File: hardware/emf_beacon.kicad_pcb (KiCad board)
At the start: 2 copper layers, 100 x 100 mm, 149 parts, among them J1 Conn_01x06, J10 Conn_01x02, J11 Conn_01x02, J12 Conn_01x02, J13 Conn_01x02, J14 Conn_01x02, J15 Conn_01x02, J16 Conn_01x06, J17 Conn_01x06, J2 RJ45_Hanrun_HR911105A_Horizon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, J3 USB_C_Receptacle_USB2.0_16P, J5 Conn_01x02, J6 Conn_01x02, J7 Conn_01x02, J8 Conn_01x02, J9 Conn_01x02, Q1 BC817W, Q10 AO3400A, Q11 AO3400A, Q12 AO3400A, Q13 DMP3013SFV, Q14 BC817W, Q2 BC817W, Q3 AO3400A, Q4 AO3400A, Q5 AO3400A, Q6 AO3400A, Q7 AO3400A, Q8 AO3400A, Q9 AO3400A, SW1 SW_DIP_x10, U1 ESP32-WROOM-32E, U10 FP6151XR-G1, U2 D3V3XA4B10LP, U3 LAN8720A, U4 MCP23017T-E/SS, U5 CA-IS3092W, U6 PCA9685PW, U8 ZTP7193MA, U9 ESP32-C3-WROOM-02

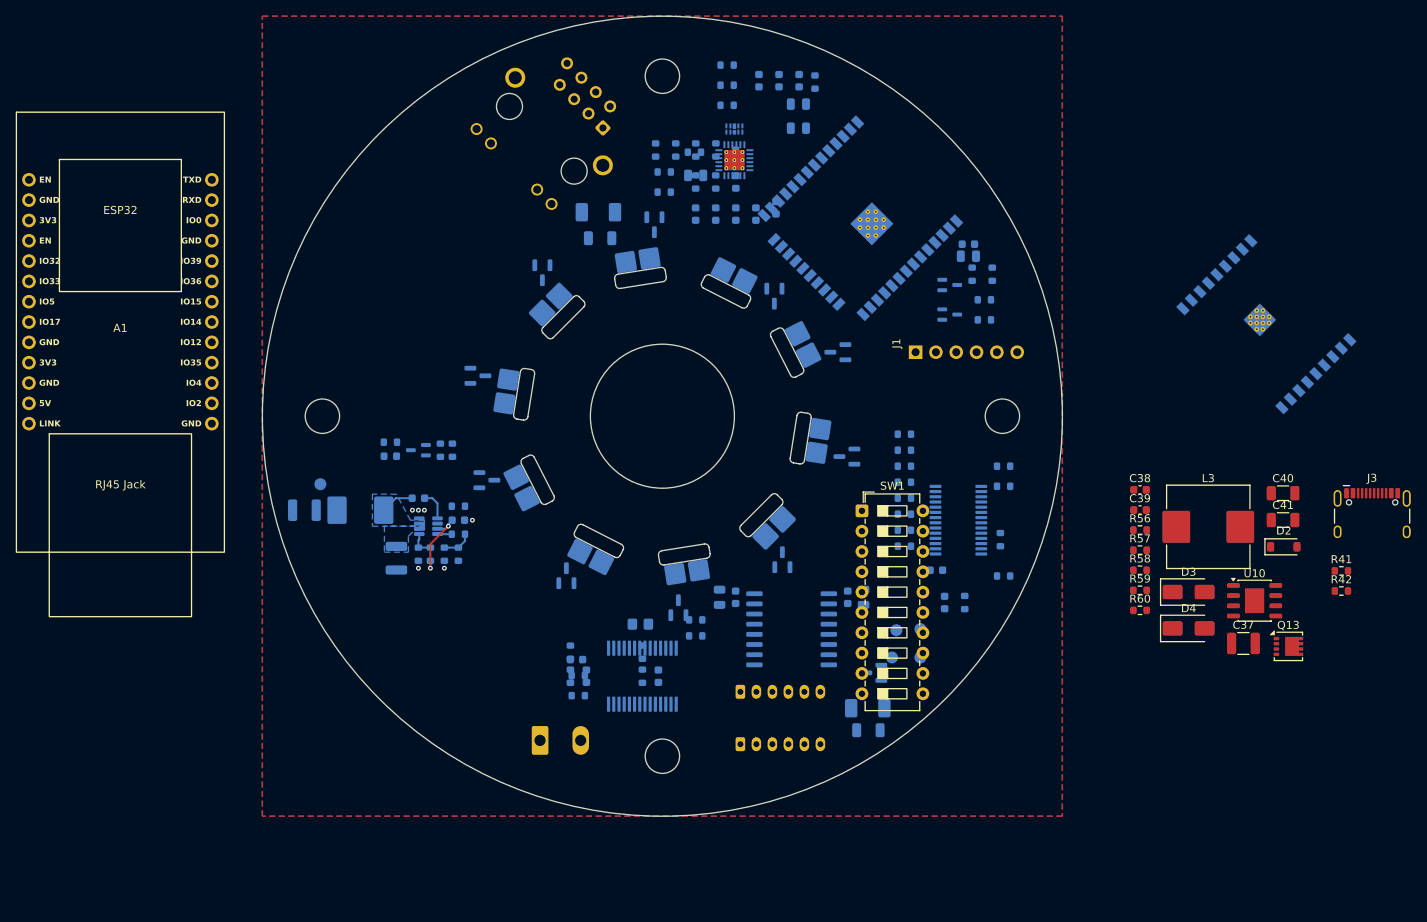
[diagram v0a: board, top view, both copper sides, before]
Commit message: removed Art-Net
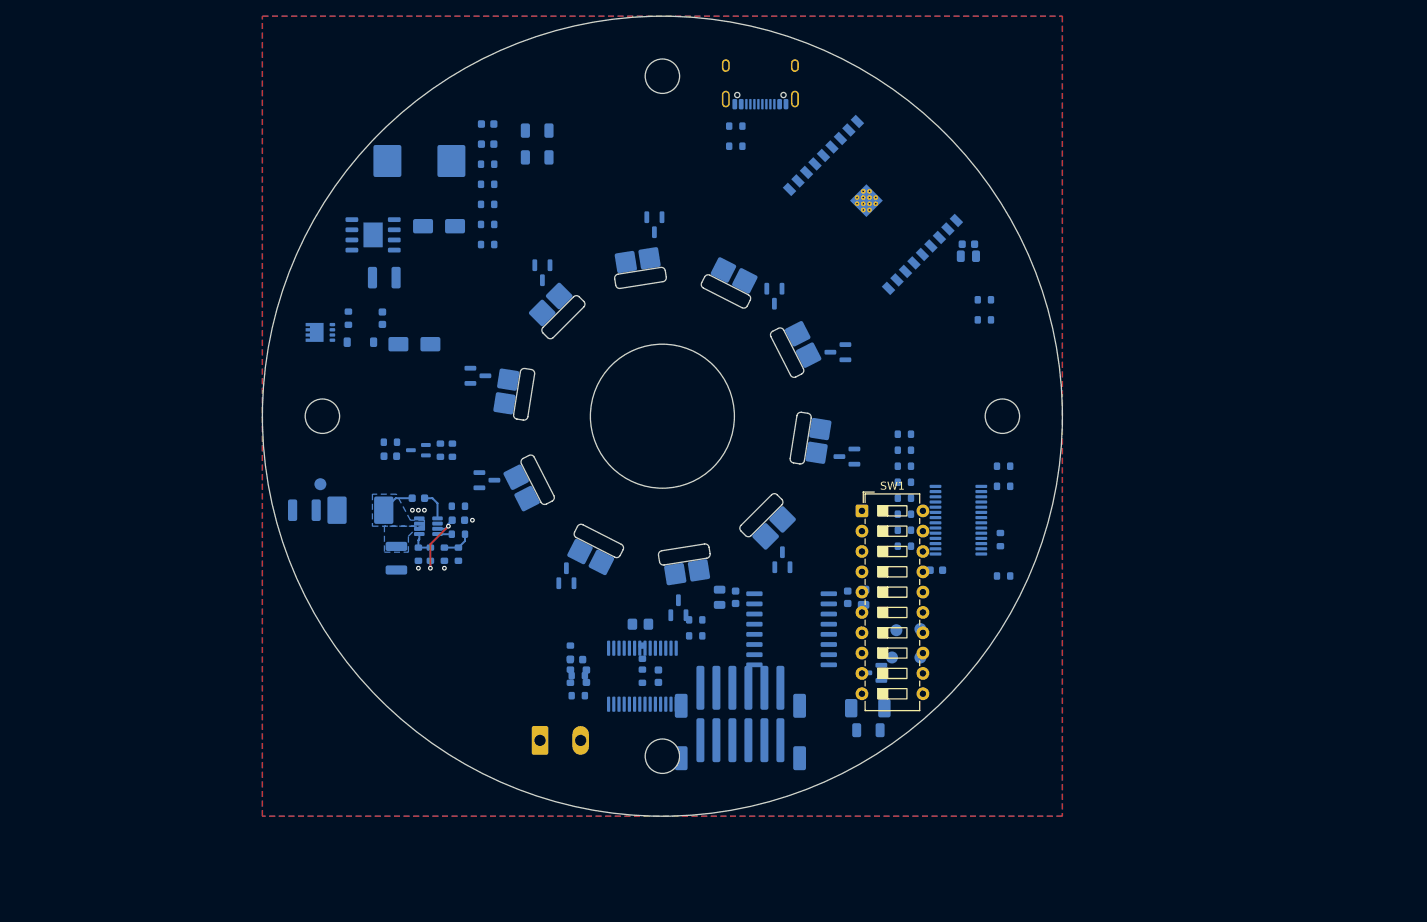
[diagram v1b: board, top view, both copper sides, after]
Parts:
- removed A1: WT32-ETH01, Pinski1_parts:WT32-ETH01
- removed C10, C7, C8, C9: 12pF, Capacitor_SMD:C_0603_1608Metric
- removed C11, C15, C16: 10uF, Capacitor_SMD:C_0805_2012Metric
- removed C12, C13, C14: 100nF, Capacitor_SMD:C_0603_1608Metric
- removed C17: 220nF, Capacitor_SMD:C_0603_1608Metric
- removed C5: 1nF 2kV, Capacitor_SMD:C_1808_4520Metric
- removed C6: 22nF, Capacitor_SMD:C_0603_1608Metric
- removed FB1: BLMxx, Inductor_SMD:L_0603_1608Metric
- removed J1: Conn_01x06, Connector_PinHeader_2.54mm:PinHeader_1x06_P2.54mm_Vertical
- removed J2: RJ45_Hanrun_HR911105A_Horizontal, Connector_RJ:RJ45_Hanrun_HR911105A_Horizontal
- removed Q1, Q2: BC817W, Package_TO_SOT_SMD:SOT-323_SC-70
- removed R10, R11, R12, R9: 49.9R, Resistor_SMD:R_0603_1608Metric
- removed R13, R14: 1k0, Resistor_SMD:R_0603_1608Metric
- removed R15: 12.1k, Resistor_SMD:R_0603_1608Metric
- removed R16, R17, R18, R19, R20, R21, R4, R5: 10k, Resistor_SMD:R_0603_1608Metric
- removed R8: 1M0, Resistor_SMD:R_1206_3216Metric
- removed U1: ESP32-WROOM-32E, RF_Module:ESP32-WROOM-32D
- removed U2: D3V3XA4B10LP, Package_DFN_QFN:Diodes_UDFN-10_1x2.5mm_P0.5mm
- removed U3: LAN8720A, Package_DFN_QFN:VQFN-24-1EP_4x4mm_P0.5mm_EP2.5x2.5mm_ThermalVias
- C37, C38, C39, C40, C41, D2, D3, D4, J3, L3, Q13, R41, R42, R56, R57, R58, R59, R60, U10: moved to B.Cu
- J16, J17: footprint Connector_JST:JST_PH_B6B-PH-K_1x06_P2.00mm_Vertical -> Connector_JST:JST_PH_B6B-PH-SM4-TB_1x06-1MP_P2.00mm_Vertical
- moved Q13 127.2 mm to (107.2, 89.5), turned to 180 degrees
- moved U10 119.3 mm to (113.8, 77.3), turned to 180 degrees
- moved D2 118.2 mm to (112.2, 90.8), turned to 180 degrees
- moved C37 116.7 mm to (115.2, 82.7), turned to 180 degrees
- moved L3 108.7 mm to (119.6, 68.1), turned to 180 degrees
- moved D3 104.3 mm to (122.1, 76.2), turned to 180 degrees
- moved C40 103.7 mm to (134.3, 64.3), turned to 180 degrees
- moved C41 103.7 mm to (134.3, 67.7), turned to 180 degrees
- moved D4 103.1 mm to (119.0, 91.0), turned to 180 degrees
- moved J3 94.9 mm to (162.2, 57.2)
- moved R41 93.9 mm to (159.2, 63.7), turned to 180 degrees
- moved R42 93.9 mm to (159.2, 66.2), turned to 180 degrees
- moved C38 93.5 mm to (128.2, 63.5), turned to 180 degrees
- moved C39 93.5 mm to (128.2, 66.0), turned to 180 degrees
- moved R56 93.5 mm to (128.2, 68.5), turned to 180 degrees
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
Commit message: clean up
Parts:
- removed Q14: BC817W, Package_TO_SOT_SMD:SOT-323_SC-70
- added C25: 100nF, Capacitor_SMD:C_0603_1608Metric, B.Cu at (150.2, 65.4)
- added C26: 100nF, Capacitor_SMD:C_0603_1608Metric, B.Cu at (150.2, 67.9)
- added C27: 10uF, Capacitor_SMD:C_0805_2012Metric, B.Cu at (145.9, 70.0)
- added D5: SS34, Diode_SMD:D_SMA, B.Cu at (155.0, 66.5)
- added Q12: AO3400A, Package_TO_SOT_SMD:SOT-23, B.Cu at (119.7, 104.0)
- added R41: 10k, Resistor_SMD:R_0603_1608Metric, B.Cu at (150.2, 70.4)
- added R42: 10k, Resistor_SMD:R_0603_1608Metric, B.Cu at (183.2, 83.5)
- added R43: 10k, Resistor_SMD:R_0603_1608Metric, B.Cu at (186.2, 82.7)
- added SW2: SW_Push, Button_Switch_SMD:SW_SPST_B3U-1000P, B.Cu at (145.2, 66.3)
- R9: renamed from R23; footprint Resistor_SMD:R_0805_2012Metric_Pad1.20x1.40mm_HandSolder -> Resistor_SMD:R_0805_2012Metric
- moved R1 5.33 mm to (164.5, 64.0), turned to -90 degrees
- moved R2 2.61 mm to (160.5, 64.0), turned to -90 degrees
- renumbered C3 to C1, C23 to C10, C24 to C11, C27 to C14, C29 to C16, C31 to C17, C37 to C18, C38 to C19, C4 to C2, C39 to C20, C33 to C21, C40 to C22, C35 to C23, C41 to C24, C2 to C3, C1 to C4, C18 to C5, C19 to C6, C20 to C7, C21 to C8, C22 to C9, D4 to D3, D3 to D4, J3 to J1, J11 to J10, J12 to J11, J13 to J12, J14 to J13, J15 to J14, J16 to J2, J17 to J3, J5 to J4, J6 to J5, J7 to J6, J8 to J7, J9 to J8, J10 to J9, L3 to L1, Q3 to Q1, Q12 to Q10, Q13 to Q11, Q4 to Q2, Q5 to Q3, Q6 to Q4, Q7 to Q5, Q8 to Q6, Q9 to Q7, Q10 to Q8, Q11 to Q9, R41 to R1, R24 to R10, R25 to R11, R26 to R12, R27 to R13, R28 to R14, R29 to R15, R30 to R16, R31 to R17, R32 to R18, R33 to R19, R42 to R2, R34 to R20, R35 to R21, R36 to R22, R37 to R23, R38 to R24, R39 to R25, R40 to R26, R56 to R27, R44 to R28, R45 to R29, R46 to R30, R57 to R31, R58 to R32, R48 to R33, R59 to R34, R60 to R35, R51 to R36, R52 to R37, R53 to R38, R54 to R39, R6 to R4, R55 to R40, R7 to R5, R1 to R6, R2 to R7, R22 to R8, TP7 to TP5, U9 to U1, U4 to U2, U5 to U3, U6 to U4, U8 to U5, U10 to U6
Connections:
- R4 pad 2: /CTRL/I2C_SCL -> /CTRL/I2C_SDA
- R5 pad 2: /CTRL/I2C_SDA -> /CTRL/I2C_SCL
- R6 pad 1: VCC -> VDC
- U1 pad 10: /CTRL/DMX_DE/~{RE} -> unconnected-(U1-IO10-Pad10)
- U1 pad 2: unconnected-(U9-EN-Pad2) -> /CTRL/ESP_EN
- U1 pad 5: unconnected-(U9-IO6-Pad5) -> /CTRL/DMX_DE/~{RE}
- U1 pad 7: unconnected-(U9-IO8-Pad7) -> Net-(U1-IO8)

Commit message: updating readme
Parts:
- moved SW1 56.2 mm to (212.9, 153.3), turned to 135 degrees
- moved R16 54.6 mm to (233.0, 102.2), turned to -90 degrees
- moved R17 52.6 mm to (231.5, 102.2), turned to -90 degrees
- moved R18 50.7 mm to (230.0, 102.2), turned to -90 degrees
- moved R19 48.9 mm to (228.5, 102.2), turned to -90 degrees
- moved R20 47.1 mm to (227.0, 102.2), turned to -90 degrees
- moved R21 45.4 mm to (225.5, 102.2), turned to -90 degrees
- moved U4 45.4 mm to (229.0, 95.8), turned to 90 degrees
- moved R22 43.8 mm to (224.0, 102.2), turned to -90 degrees
- moved R23 42.2 mm to (222.5, 102.2), turned to -90 degrees
- moved R24 32.1 mm to (221.6, 94.8), turned to 180 degrees
- moved R25 31.7 mm to (221.6, 93.2), turned to 180 degrees
- moved R41 14.3 mm to (142.2, 58.5), turned to 90 degrees
- moved C26 13.5 mm to (140.5, 58.5), turned to -90 degrees
- moved SW2 12.1 mm to (142.8, 54.5)
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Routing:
- net /LEDS/LED1: track 0.00 -> 4.62 mm
- net /LEDS/LED8: track 0.00 -> 4.52 mm
- net /LEDS/LED2: track 0.00 -> 3.77 mm
- net /LEDS/LED7: track 0.00 -> 3.67 mm
- net /LEDS/LED3: track 0.00 -> 3.36 mm
- net /LEDS/LED6: track 0.00 -> 3.32 mm
- net /LEDS/LED4: track 0.00 -> 3.01 mm
- net /LEDS/LED5: track 0.00 -> 2.97 mm

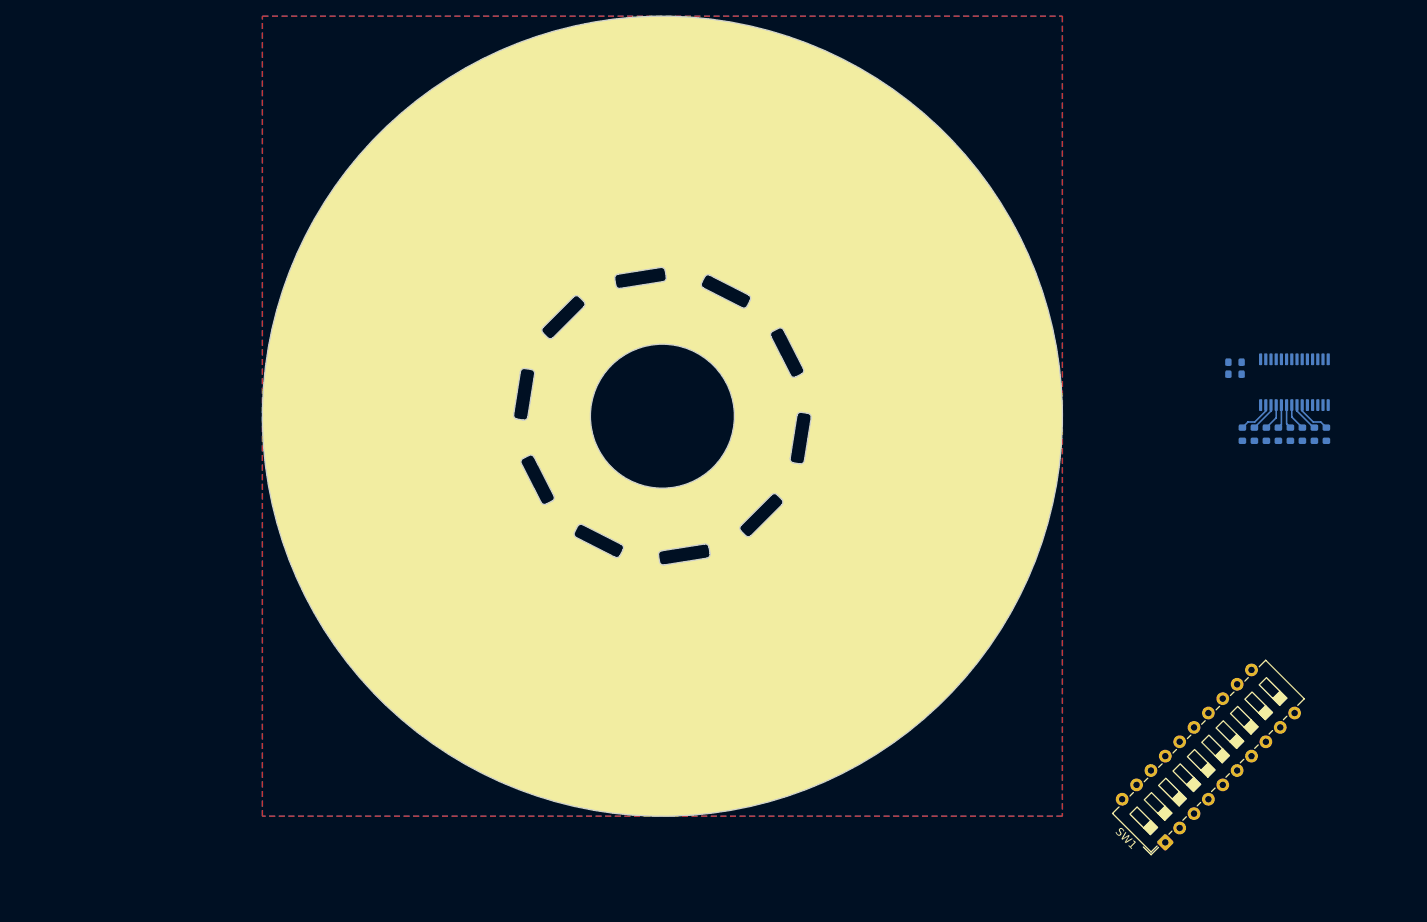
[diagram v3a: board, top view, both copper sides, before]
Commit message: updating thermistor and GPIO expander
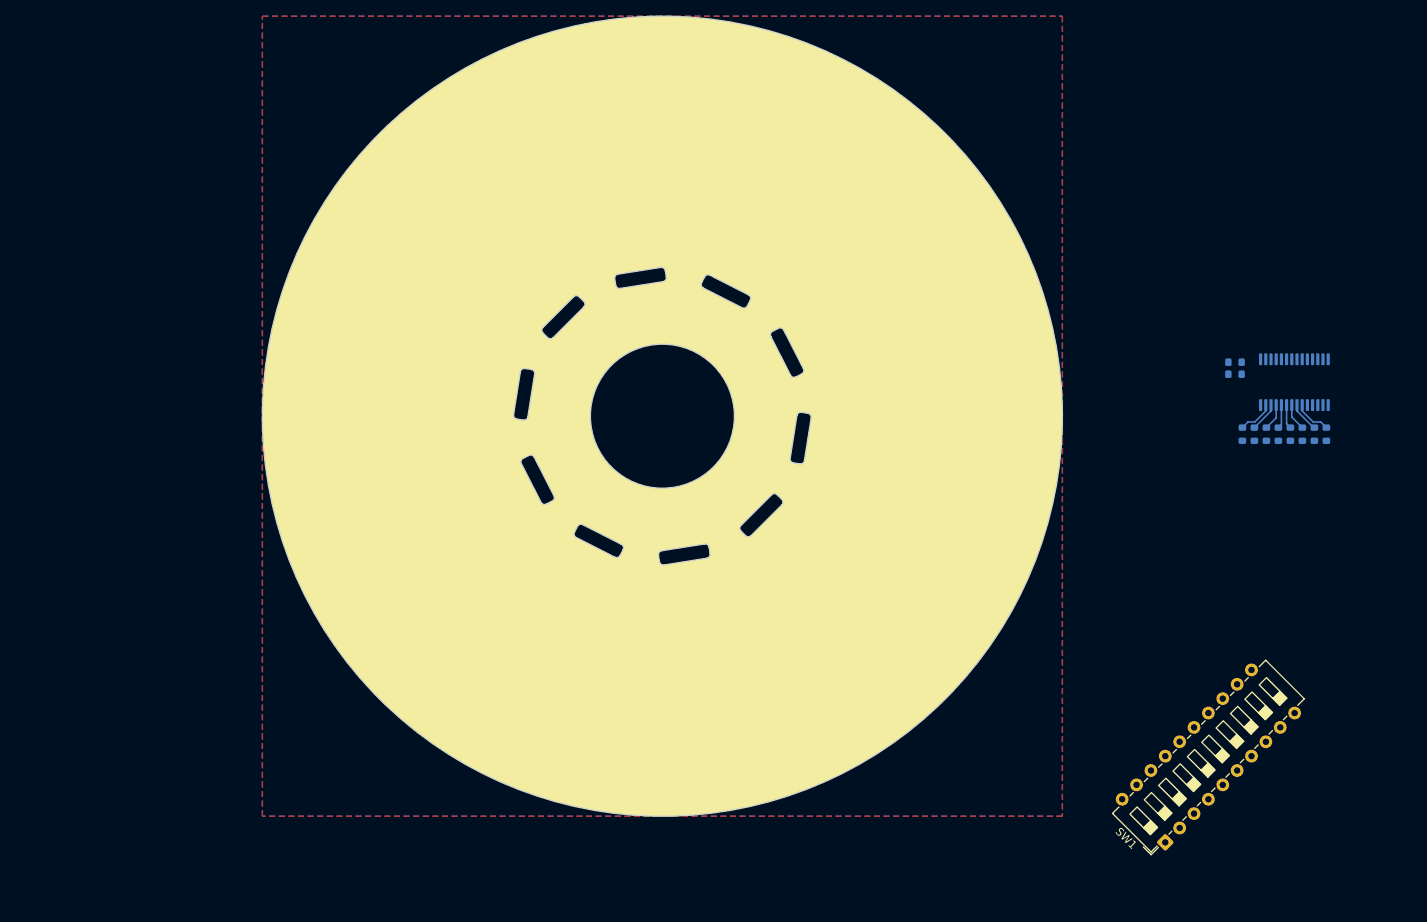
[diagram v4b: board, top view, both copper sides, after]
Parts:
- R6: value 43k -> 62k
- TH1: value Thermistor_NTC -> NCP15XH103F03RC
- moved C27 53.1 mm to (190.0, 91.2), turned to 0 degrees
- moved R3 42.5 mm to (188.5, 121.2)
- moved C3 39.8 mm to (188.5, 124.5)
- moved TH1 39.6 mm to (186.8, 124.5)
- moved R14 32.8 mm to (190.0, 87.2)
- moved R4 32.0 mm to (169.9, 63.2)
- moved R5 31.4 mm to (169.9, 61.5)
- moved R42 7.52 mm to (190.0, 88.8)
- moved R43 4.00 mm to (190.0, 85.8), turned to 0 degrees
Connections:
- net /CTRL/BOOT renamed /CTRL/ESP_~{BOOT}
- net /CTRL/ESP_EN renamed /CTRL/ESP_~{RST}
- R3 pad 1: /CTRL/TEMP_MON -> +3V3
- R3 pad 2: GND -> /CTRL/TEMP_MON
- TH1 pad 1: +3V3 -> /CTRL/TEMP_MON
- TH1 pad 2: /CTRL/TEMP_MON -> GND
- U2 pad 1: /DMX512/DMX_ADDR0 -> /DMX512/DMX_ADDR7
- U2 pad 2: /DMX512/DMX_ADDR1 -> /DMX512/DMX_ADDR8
- U2 pad 21: /DMX512/DMX_ADDR8 -> /DMX512/DMX_ADDR0
- U2 pad 22: unconnected-(U2-GPA1-Pad22) -> /DMX512/DMX_ADDR1
- U2 pad 23: unconnected-(U2-GPA2-Pad23) -> /DMX512/DMX_ADDR2
- U2 pad 24: unconnected-(U2-GPA3-Pad24) -> /DMX512/DMX_ADDR3
- U2 pad 25: unconnected-(U2-GPA4-Pad25) -> /DMX512/DMX_ADDR4
- U2 pad 26: unconnected-(U2-GPA5-Pad26) -> /DMX512/DMX_ADDR5
- U2 pad 27: unconnected-(U2-GPA6-Pad27) -> /DMX512/DMX_ADDR6
- U2 pad 3: /DMX512/DMX_ADDR2 -> unconnected-(U2-GPB2-Pad3)
- U2 pad 4: /DMX512/DMX_ADDR3 -> unconnected-(U2-GPB3-Pad4)
- U2 pad 5: /DMX512/DMX_ADDR4 -> unconnected-(U2-GPB4-Pad5)
- U2 pad 6: /DMX512/DMX_ADDR5 -> unconnected-(U2-GPB5-Pad6)
- U2 pad 7: /DMX512/DMX_ADDR6 -> unconnected-(U2-GPB6-Pad7)
- U2 pad 8: /DMX512/DMX_ADDR7 -> unconnected-(U2-GPB7-Pad8)
